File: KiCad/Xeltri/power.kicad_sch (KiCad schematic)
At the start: 110 parts, among them J1 PJ-035DH, Q1 AOD407, U10 SY8843QWC, U11 RT9013-18GB, U12 RT9013-12GB, U13 TPS22966DPUR, U14 TPS22966DPUR, U15 TPS22966DPUR, U16 TPS22966DPUR, U3 TPS56637RPAR, U4 TPS56637RPAR, U7 SY8843QWC, U8 SY8843QWC, U9 SY8843QWC

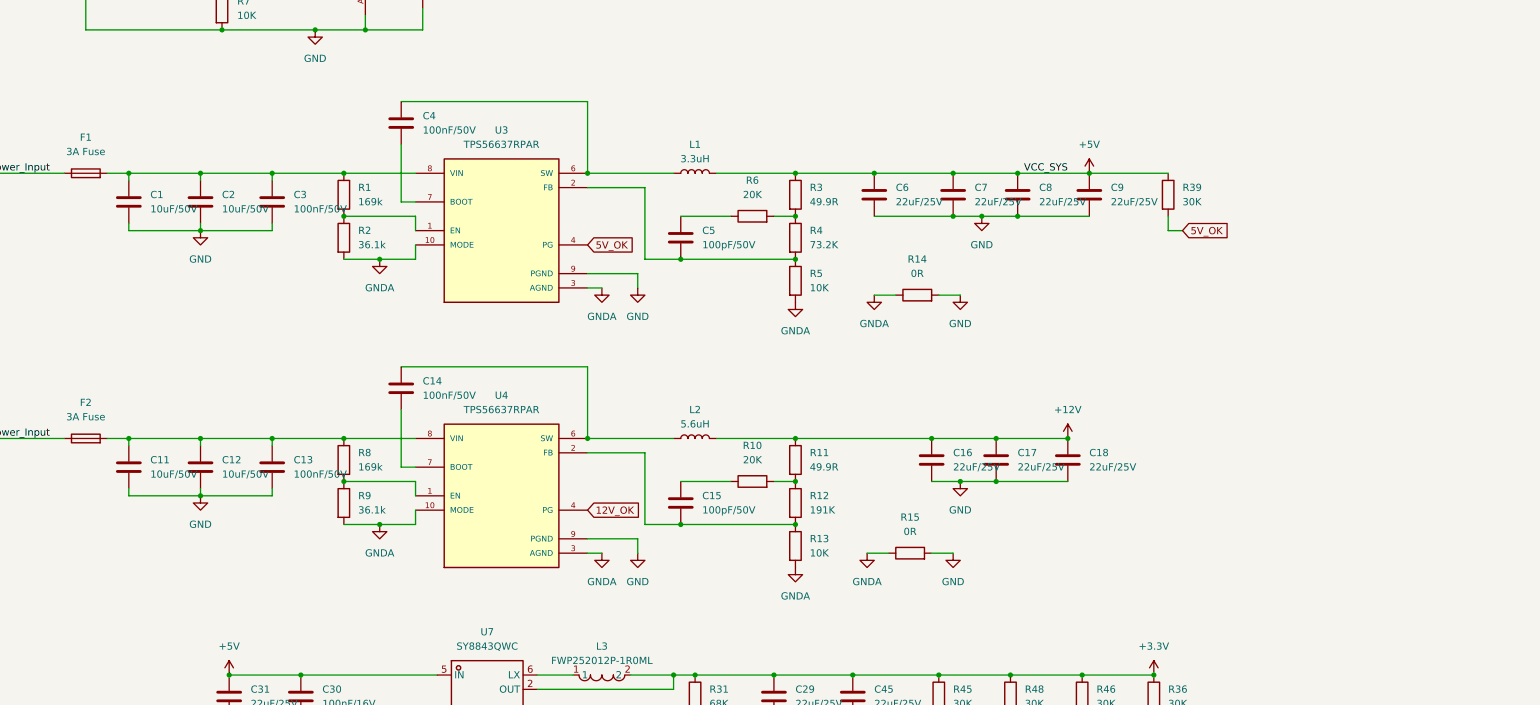
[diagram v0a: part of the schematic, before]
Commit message: Lay out STM32 power decoupling and add USB FS plus 24 V CIN ceramics.
USB VDD33/VDD50 share local 100 nF + 1 µF on 3.3 V; VBAT keeps a local 100 nF until the cell and diode are placed.

Co-authored-by: Cursor <cursoragent@cursor.com>
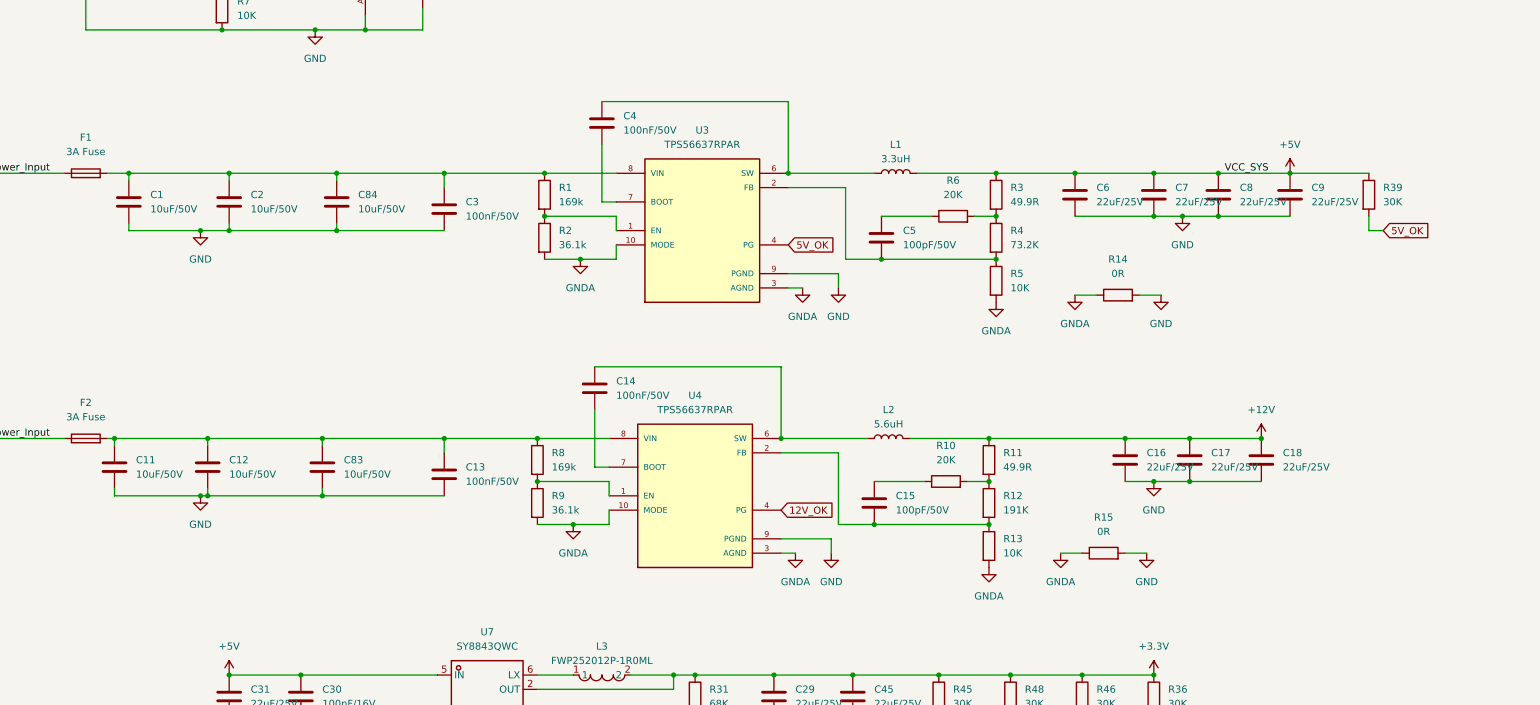
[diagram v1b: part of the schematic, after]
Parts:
- added C83, C84: 10uF/50V, Capacitor_SMD:C_1206_3216Metric, symbol Device:C
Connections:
- net GND: now also C83.2, C84.2
- net at C11.1, C12.1, C13.1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: now also C83.1
- net at C1.1, C2.1, C3.1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: now also C84.1
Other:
- moved on the sheet: C11, C12, C13, C14, C15, C16, C17, C18, C2, C3, C4, C5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

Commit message: Match the six-layer stackup to JLC06161H-3313 and update FPGA power wiring.
Co-authored-by: Cursor <cursoragent@cursor.com>
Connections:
- net +3.3V: no longer U13.4 (VBIAS), U14.4 (VBIAS)
- net +5V: now also U13.4 (VBIAS), U14.4 (VBIAS), U15.4 (VBIAS), U16.4 (VBIAS)
- net GND: now also U13.11 (GND), U13.15 (EP), U14.11 (GND), U14.15 (EP), U15.11 (GND), U15.15 (EP), U16.11 (GND), U16.15 (EP)
